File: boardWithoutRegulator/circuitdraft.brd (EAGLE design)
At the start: 63 x 37 mm, 49 parts, among them IC1 BQ25887RGER, IC2 TPS54627DDAR, Q1 16 MHz

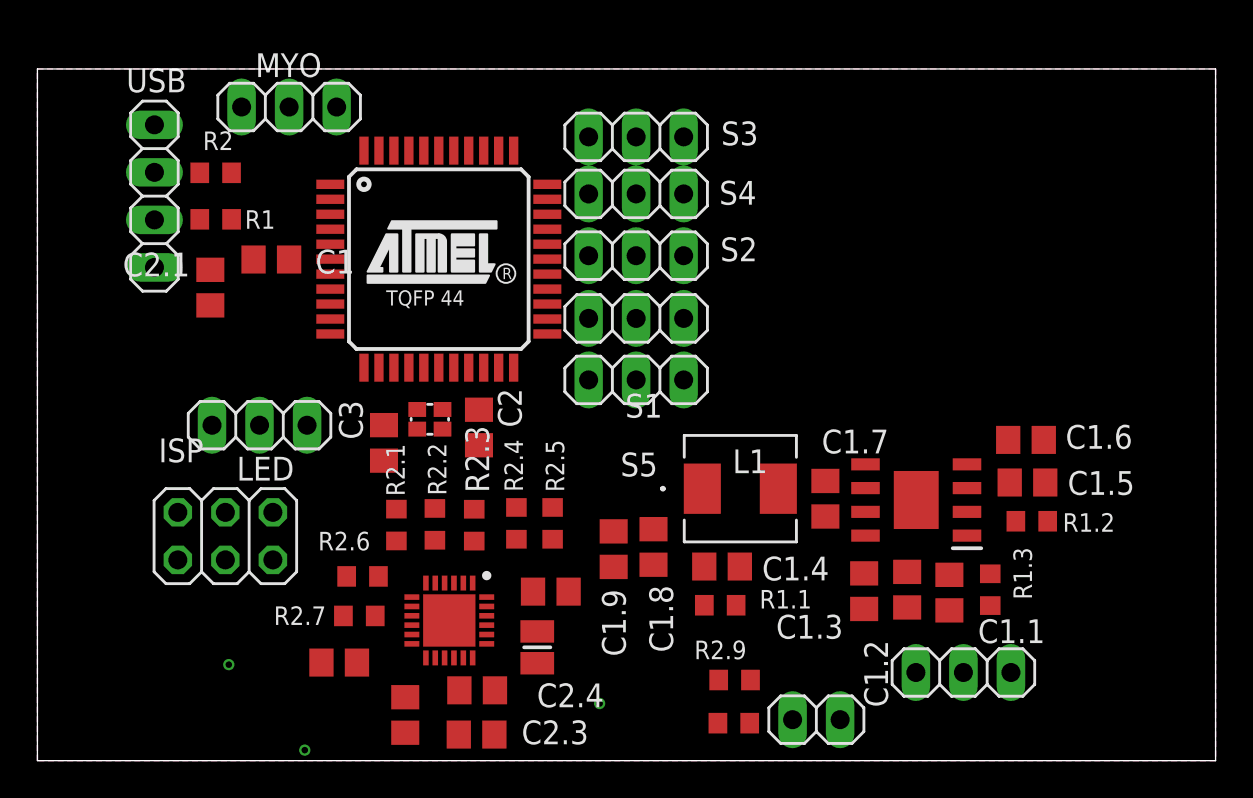
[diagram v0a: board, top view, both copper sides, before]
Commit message: Started to route and made power more centralized
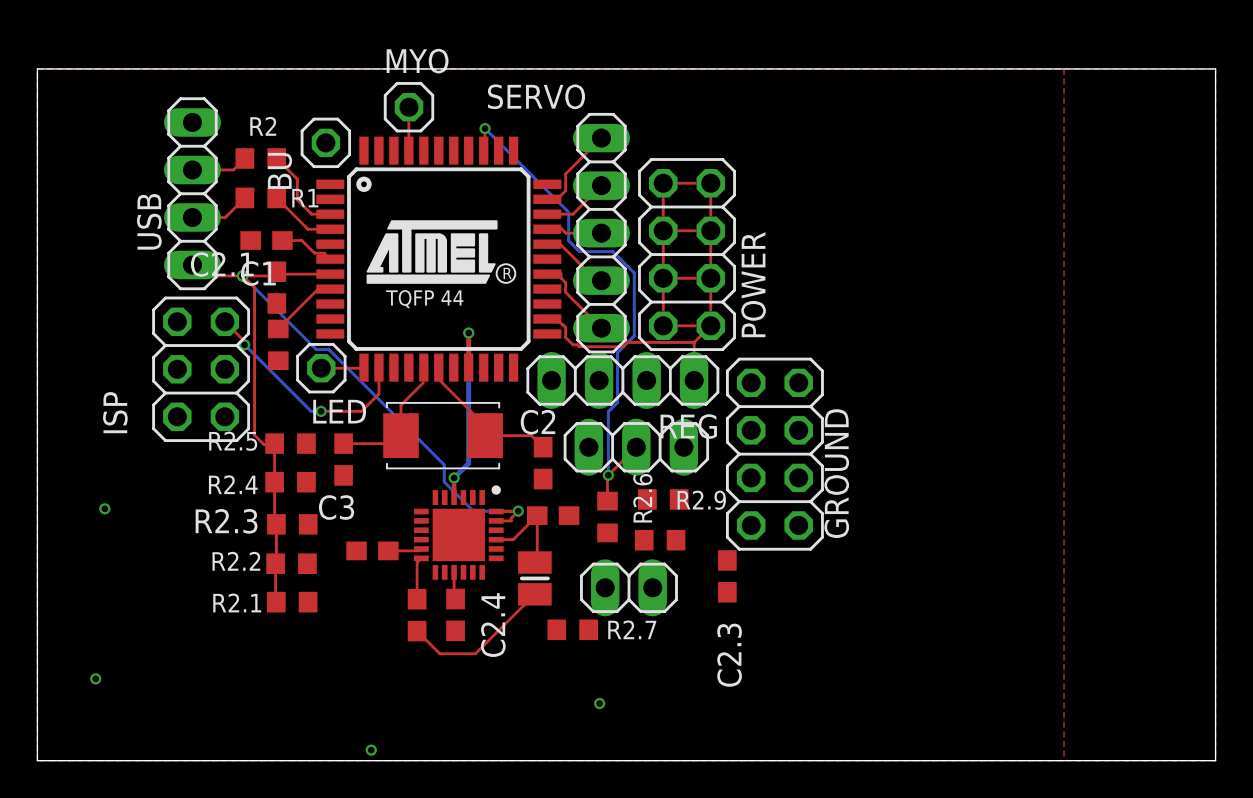
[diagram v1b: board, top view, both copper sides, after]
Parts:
- removed C1.1, C1.2: 10 uF, rcl:C0805
- removed C1.3: .1 uF, rcl:C0805
- removed C1.4: 10 pF, rcl:C0805
- removed C1.5: 1 uF, rcl:C0805
- removed C1.6: 8200 pF, rcl:C0805
- removed C1.7: 0.1 uF, rcl:C0805
- removed C1.8, C1.9: 22 uF, rcl:C0805
- removed IC2: TPS54627DDAR, TPS54627DDAR:SOIC127P600X170-9N
- removed L1: IHLP2020CZER3R3M01, ind2:IND_IHLP-2020CZ
- removed R1.1: 124000 Ohms, rcl:R0603
- removed R1.2: 22100 Ohms, rcl:R0603
- removed R1.3: 10000 Ohms, rcl:R0603
- removed S1, S2, S3, S4, S5: (no value), pinhead:1X03
- added BU: (no value), pinhead:1X01
- added GROUND, POWER: (no value), pinhead:2X04
- added RBUTTON: 220 Ohm, rcl:R0603
- added REG: (no value), pinhead:1X04
- added SERVO: (no value), pinhead:1X05
- C1, C2, C2.1, C2.2, C2.3, C2.4, C2.5, C2.6, C3: device rcl:C0805 -> rcl:C0603
- LED, MYO: device pinhead:1X03 -> pinhead:1X01
- Q1: device crystal-geyer_V1_0:2.0X1.6_KX-5 -> SamacSys_Parts:ECS2501823GJGNTR
- moved BATIO 21.2 mm to (43.0, 16.8), turned to 0 degrees
- moved C2.3 15.8 mm to (47.9, 9.85), turned to 90 degrees
- moved R2.5 14.6 mm to (24.5, 16.9), turned to 180 degrees
- moved R2.6 13.5 mm to (41.5, 13.0), turned to 270 degrees
- moved R2.4 12.3 mm to (24.5, 14.9), turned to 180 degrees
- moved TS 12.2 mm to (42.6, 9.24), turned to 180 degrees
- moved R2.7 11.4 mm to (39.6, 7.00), turned to 180 degrees
- moved R2.8 10.5 mm to (44.3, 11.8)
- moved R2.9 10.4 mm to (44.5, 14.0)
- moved R2.3 9.72 mm to (24.6, 12.6), turned to 180 degrees
- moved ISP 9.01 mm to (19.7, 20.9), turned to 90 degrees
- moved R2.2 7.95 mm to (24.6, 10.5), turned to 180 degrees
- moved R2.1 6.93 mm to (24.6, 8.47), turned to 180 degrees
- moved MYO 6.41 mm to (30.9, 34.9)
- moved C2.2 6.23 mm to (28.9, 11.2)
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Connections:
- removed net AGND: C1.6.2, R1.2.2
- removed net N$1: IC2.1, R1.3.2
- removed net N$11: C1.4.1, IC2.2, R1.1.2, R1.2.1
- removed net N$13: C1.5.1, IC2.3
- removed net N$14: C1.7.1, IC2.6, L1.2
- removed net N$15: C1.7.2, IC2.7
- removed net N$9: C1.6.1, IC2.4
- new net ENABLE: REG.4
- new net INTERRUPT: BU.1, RBUTTON.1, U$1.8
- net B+: now also REG.3; no longer C1.1.2, C1.2.2, C1.3.2, IC2.8, R1.3.1
- net DATAIN: now also LED.1; no longer LED.3
- net GND: now also GROUND.1, GROUND.2, GROUND.3, GROUND.4, GROUND.5, GROUND.6, GROUND.7, GROUND.8, IC1.25, RBUTTON.2, REG.2; no longer C1.1.1, C1.2.1, C1.3.1, C1.5.2, C1.8.2, C1.9.2, IC2.5, IC2.9, LED.2, MYO.2, S1.3, S2.3, S3.3, S4.3, S5.3
- net MYOSIGNAL: now also MYO.1; no longer MYO.3
- net N$6: now also Q1.2; no longer Q1.3
- net POWER: now also POWER.1, POWER.2, POWER.3, POWER.4, POWER.5, POWER.6, POWER.7, POWER.8, REG.1; no longer C1.4.2, C1.8.1, C1.9.1, L1.1, LED.1, MYO.1, R1.1.1, S1.2, S2.2, S3.2, S4.2, S5.2
- net SIGNAL1: now also SERVO.4; no longer S1.1
- net SIGNAL2: now also SERVO.3; no longer S2.1
- net SIGNAL3: now also SERVO.1; no longer S3.1
- net SIGNAL4: now also SERVO.2; no longer S4.1
- net SIGNAL5: now also SERVO.5; no longer S5.1
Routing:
- net VBUS: track 0.00 -> 49.5 mm, vias 0 -> 3
- net POWER: track 0.00 -> 37.1 mm
- net MIDDLE: track 0.00 -> 28.2 mm, vias 0 -> 2
- net RST: track 0.00 -> 12.1 mm, vias 0 -> 2
- net SDA: track 0.00 -> 11.0 mm, vias 0 -> 2
- net N$18: track 0.00 -> 8.11 mm
- net N$6: track 0.00 -> 7.48 mm
- net N$5: track 0.00 -> 6.56 mm
- net N$21: track 0.00 -> 5.29 mm
- net N$2: track 0.00 -> 4.25 mm
- net SIGNAL3: track 0.00 -> 4.25 mm
- net SIGNAL5: track 0.00 -> 3.82 mm
- net INTERRUPT: track 0.00 -> 3.66 mm
- net N$4: track 0.00 -> 3.56 mm
- net D+: track 0.00 -> 3.24 mm
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
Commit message: More Routing
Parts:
- moved TS 21.3 mm to (21.7, 5.30)
- moved R2.8 19.3 mm to (26.1, 5.49), turned to 0 degrees
- moved R2.9 18.7 mm to (26.2, 10.3), turned to 0 degrees
- moved C2.3 11.5 mm to (36.9, 13.2), turned to 0 degrees
- moved R2.1 4.20 mm to (20.4, 8.22)
- moved R2.2 4.20 mm to (20.4, 10.3)
- moved R2.3 4.07 mm to (20.6, 12.4)
- moved R2.4 3.82 mm to (20.7, 14.6)
- moved C2.2 3.70 mm to (27.0, 8.04)
- moved C2.4 3.66 mm to (32.1, 4.36)
- moved C2.5 3.66 mm to (30.0, 4.35)
- moved R2.5 3.31 mm to (21.2, 16.7)
- moved C2.6 2.74 mm to (37.6, 10.6)
- moved IC1 2.74 mm to (32.5, 9.52)
- moved L2 2.74 mm to (36.6, 7.20)
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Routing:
- net N$7: track 0.00 -> 96.1 mm
- net STAT: track 0.00 -> 31.4 mm, vias 0 -> 2
- net B+: track 0.00 -> 18.2 mm, vias 0 -> 2
- net SDA: track 11.0 -> 27.0 mm
- net N$3: track 0.00 -> 15.5 mm, vias 0 -> 2
- net SCL: track 0.00 -> 15.0 mm
- net TS: track 0.00 -> 12.6 mm
- net INT: track 0.00 -> 11.5 mm
- net MIDDLE: track 28.2 -> 38.6 mm
- net N$18: track 8.11 -> 13.2 mm
- net N$19: track 1.81 -> 5.98 mm
- net VBUS: track 49.5 -> 52.2 mm, vias 3 -> 2
- net BTST: track 2.28 -> 3.28 mm
- net N$20: track 1.46 -> 2.39 mm

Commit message: Routhing
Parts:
- moved ISP 0.25 mm to (19.5, 20.9)
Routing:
- net N$7: track 96.1 -> 38.6 mm
- net SCL: track 15.0 -> 43.0 mm
- net INT: track 11.5 -> 34.1 mm, vias 0 -> 4
- net N$10: track 0.00 -> 18.9 mm, vias 0 -> 2
- net UGND: track 0.00 -> 11.4 mm, vias 0 -> 2
- net INTERRUPT: track 3.66 -> 14.5 mm
- net VBUS: track 52.2 -> 58.3 mm, vias 2 -> 4
- net B+: track 18.2 -> 22.0 mm
- net SIGNAL2: track 2.26 -> 4.89 mm
- net SIGNAL1: track 2.95 -> 4.21 mm
- net N$6: track 7.48 -> 8.54 mm
- net SDA: track 27.0 -> 27.9 mm
- net N$5: track 6.45 -> 7.27 mm
- net SIGNAL4: track 2.79 -> 3.53 mm
- net SIGNAL5: track 3.82 -> 4.45 mm
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
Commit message: Finished routuing?
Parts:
- moved RBUTTON 9.37 mm to (15.5, 26.4), turned to 180 degrees
- moved C2.1 8.95 mm to (15.5, 28.7), turned to 0 degrees
- moved GROUND 8.53 mm to (45.3, 9.53)
- moved ISP 1.65 mm to (17.8, 20.9)
- moved SERVO 0.65 mm to (41.8, 28.3)
- moved C2.6 0.51 mm to (37.6, 10.1)
- moved POWER 0.38 mm to (46.1, 27.1)
- moved C1 0.36 mm to (23.0, 28.1)
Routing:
- net N$7: track 38.6 -> 15.3 mm, vias 0 -> 2
- net MOSI: track 0.00 -> 17.1 mm, vias 0 -> 2
- net MISO: track 0.00 -> 9.37 mm
- net SCK: track 0.00 -> 8.98 mm
- net INTERRUPT: track 14.5 -> 21.8 mm
- net INT: track 34.1 -> 36.9 mm
- net RST: track 12.3 -> 13.9 mm
- net UGND: track 11.4 -> 12.9 mm
- net STAT: track 31.4 -> 32.2 mm
- net MIDDLE: track 38.6 -> 39.4 mm
- net N$21: track 5.29 -> 4.57 mm
- net SIGNAL4: track 3.53 -> 4.22 mm
- net SIGNAL2: track 4.89 -> 5.47 mm
- net SIGNAL1: track 4.21 -> 4.71 mm
- net VBUS: track 58.3 -> 58.0 mm, vias 4 -> 5
